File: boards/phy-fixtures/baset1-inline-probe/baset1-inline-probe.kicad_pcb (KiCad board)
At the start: 4 copper layers, 57.5 x 40.5 mm, 15 parts, among them J1 TERMINALS, J2 SMA, J3 SMA, J4 SMA, J5 SMA, J6 TERMINALS, M1 LOGO, M2 LOGO, M3 LOGO, U1 ADCB-20-82+, U2 ADCB-20-82+

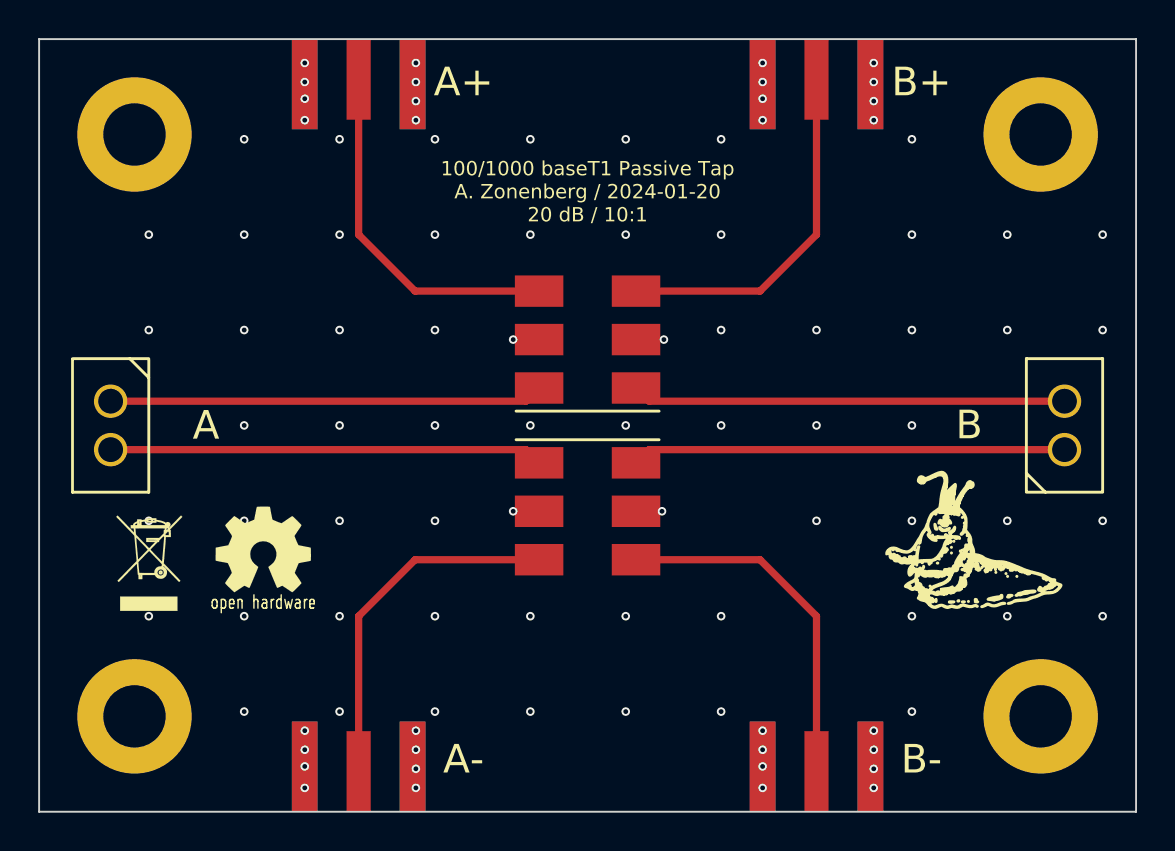
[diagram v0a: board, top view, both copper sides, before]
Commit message: Updated baset1-inline-probe to use matched coupler layout
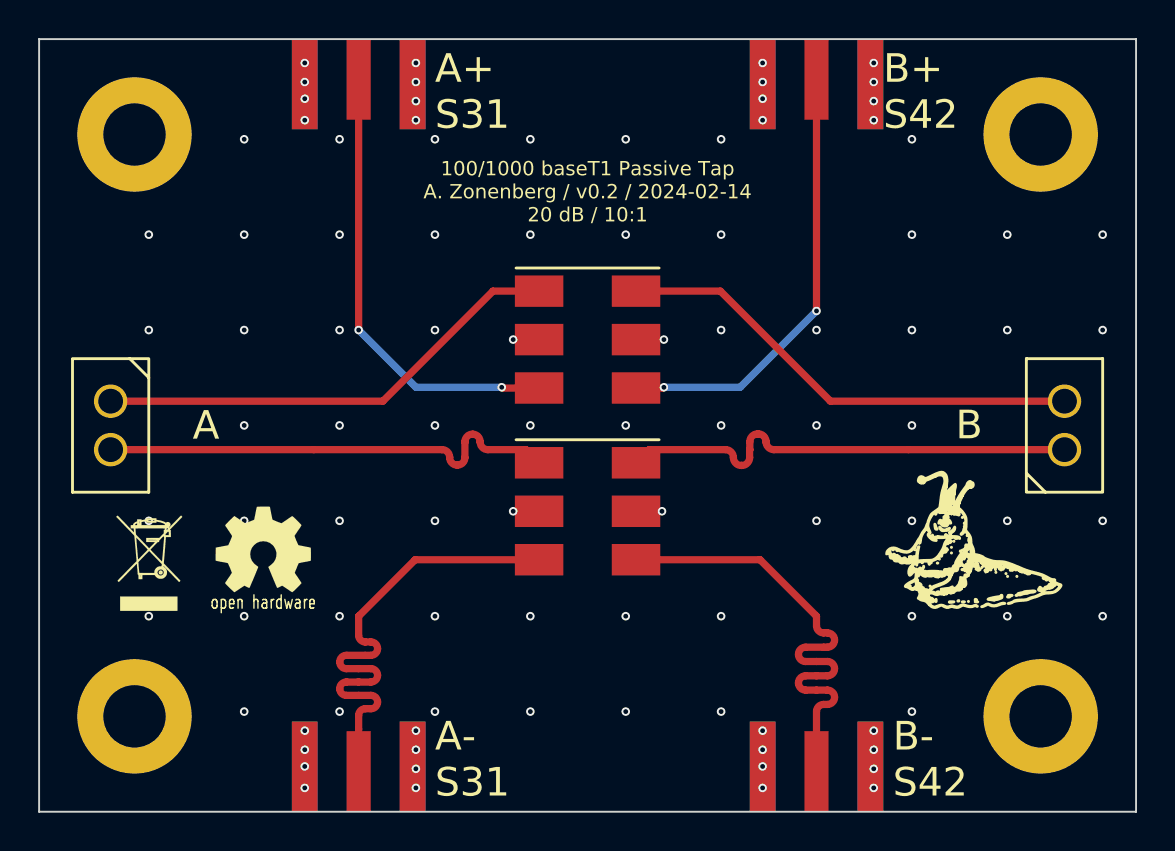
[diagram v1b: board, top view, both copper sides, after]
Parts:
- turned U1 to -90 degrees
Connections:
- U1 pad 1: /OUT_P -> /IN_P
- U1 pad 3: /REV_P -> /FWD_P
- U1 pad 4: /FWD_P -> /REV_P
- U1 pad 6: /IN_P -> /OUT_P
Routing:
- net /FWD_N: track 18.8 -> 26.8 mm
- net /REV_N: track 18.8 -> 26.2 mm
- net /FWD_P: track 18.8 -> 23.8 mm, vias 0 -> 2
- net /REV_P: track 18.8 -> 23.3 mm, vias 0 -> 2
- net /OUT_N: track 22.7 -> 24.9 mm
- net /IN_N: track 22.7 -> 24.9 mm
- net /IN_P: track 22.7 -> 24.9 mm
- net /OUT_P: track 22.7 -> 24.9 mm
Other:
- board text added: "100/1000 baseT1 Passive Tap A. Zonenberg / v0.2 / 2024-02-14 20 dB / 10:1"
- board text added: "A+ S31"
- board text added: "A- S31"
- board text added: "B+ S42"
- board text added: "B- S42"
- board text removed: "100/1000 baseT1 Passive Tap A. Zonenberg / 2024-01-20 20 dB / 10:1"
- board text removed: "A+"
- board text removed: "A-"
- board text removed: "B+"
- board text removed: "B-"
